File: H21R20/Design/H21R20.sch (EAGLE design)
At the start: 52 parts, among them IC1 ESP32-C3-MINI-1-N4, P1 HEXABIT_17.32_NO_P6_P7_P12, U1 STM32G0B1CEU6NUFQFPN48_STM32_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, X1 8MHZ

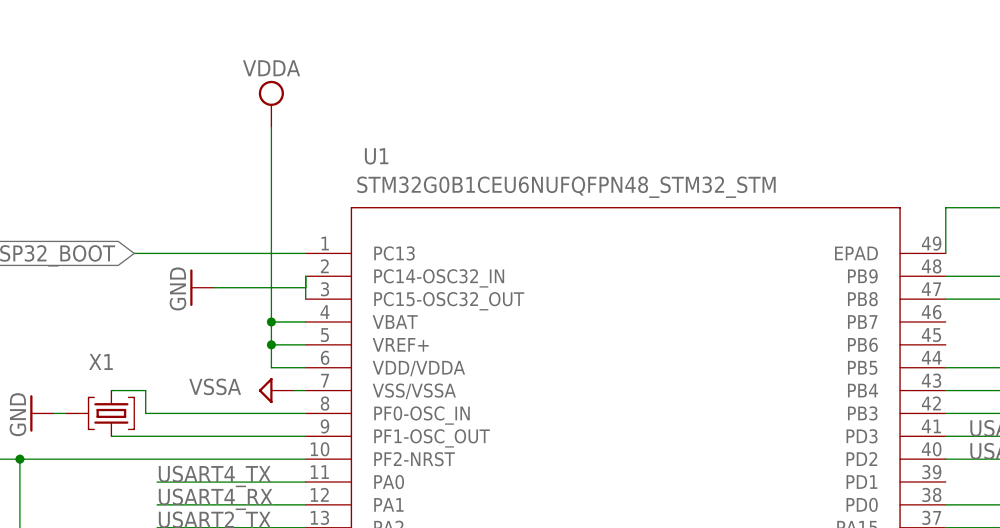
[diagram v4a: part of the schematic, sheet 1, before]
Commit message: -Improve the layout design -Change the jumber resistors footprint to 0402
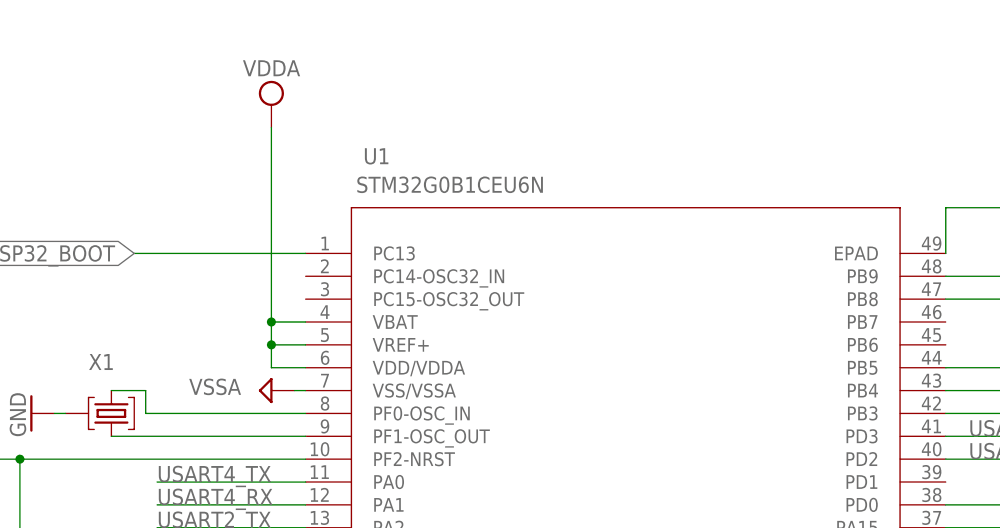
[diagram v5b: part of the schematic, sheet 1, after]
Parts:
- R11, R12, R13: device HEXABITZ_RCLS:R-0603 -> HEXABITZ_RCLS:R-0402
- U1: value STM32G0B1CEU6NUFQFPN48_STM32_STM -> STM32G0B1CEU6N; device HEXABITZ_ICs:STM32G0B1CEU6NUFQFPN48_STM32_STM -> HEXABITZ_ICs:STM32G0B1CEU6N; OCTOPART_URL https://octopart.com/stm32g0b1ceu6n-stmicroelectronics-1163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 -> (none)
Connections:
- net GND: no longer U1.PC14-OSC32_IN, U1.PC15-OSC32_OUT
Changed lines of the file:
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@@
 <?xml version="1.0" encoding="utf-8"?>
 <!DOCTYPE eagle SYSTEM "eagle.dtd">
-<eagle version="9.6.1">
+<eagle version="9.6.2">
 <drawing>
 <settings>
@@
 <layer number="1" name="Top" color="4" fill="1" visible="no" active="no"/>
 <layer number="2" name="Route2" color="1" fill="3" visible="no" active="no"/>
+<layer number="3" name="Route3" color="17" fill="1" visible="no" active="no"/>
+<layer number="4" name="Route4" color="18" fill="1" visible="no" active="no"/>
+<layer number="5" name="Route5" color="19" fill="1" visible="no" active="no"/>
+<layer number="6" name="Route6" color="25" fill="1" visible="no" active="no"/>
+<layer number="7" name="Route7" color="26" fill="1" visible="no" active="no"/>
+<layer number="8" name="Route8" color="27" fill="1" visible="no" active="no"/>
+<layer number="9" name="Route9" color="28" fill="1" visible="no" active="no"/>
+<layer number="10" name="Route10" color="29" fill="1" visible="no" active="no"/>
+<layer number="11" name="Route11" color="30" fill="1" visible="no" active="no"/>
+<layer number="12" name="Route12" color="20" fill="1" visible="no" active="no"/>
+<layer number="13" name="Route13" color="21" fill="1" visible="no" active="no"/>
+<layer number="14" name="Route14" color="22" fill="1" visible="no" active="no"/>
 <layer number="15" name="Route15" color="4" fill="6" visible="no" active="no"/>
 <layer number="16" name="Bottom" color="1" fill="1" visible="no" active="no"/>
@@
 <part name="SUPPLY12" library="supply2" library_urn="urn:adsk.eagle:library:372" deviceset="VCC" device="" value="VDDA"/>
 <part name="SUPPLY9" library="supply2" library_urn="urn:adsk.eagle:library:372" deviceset="GND1" device="" value="VSSA"/>
-<part name="U1" library="HEXABITZ_ICs" library_urn="urn:adsk.eagle:library:20064554" deviceset="STM32G0B1CEU6N" device="UFQFPN48_STM32_STM" package3d_urn="urn:adsk.eagle:package:33906703/4">
-<attribute name="OCTOPART_URL" value="https://octopart.com/stm32g0b1ceu6n-stmicroelectronics-116364672?r=sp"/>
-</part>
+<part name="U1" library="HEXABITZ_ICs" library_urn="urn:adsk.eagle:library:20064554" deviceset="STM32G0B1CEU6N" device="" package3d_urn="urn:adsk.eagle:package:39679334/7" value="STM32G0B1CEU6N"/>
 <part name="R" library="HEXABITZ_USER_INTERFACE_PARTS" library_urn="urn:adsk.eagle:library:20064563" deviceset="PINHD-1X1" device="" package3d_urn="urn:adsk.eagle:package:22485/2"/>
 <part name="JP1" library="pinhead" deviceset="PINHD-1X3" device="" package3d_urn="urn:adsk.eagle:package:22458/2"/>
@@
 <part name="RX0" library="HEXABITZ_CONNECTION_PARTS" library_urn="urn:adsk.eagle:library:27886345" deviceset="PAD4" device="" package3d_urn="urn:adsk.eagle:package:27886422/1"/>
 <part name="TX0" library="HEXABITZ_CONNECTION_PARTS" library_urn="urn:adsk.eagle:library:27886345" deviceset="PAD4" device="" package3d_urn="urn:adsk.eagle:package:27886422/1"/>
-<part name="R11" library="HEXABITZ_RCLS" library_urn="urn:adsk.eagle:library:20064561" deviceset="R-0603" device="" package3d_urn="urn:adsk.eagle:package:1435818/5" value="0R">
+<part name="R11" library="HEXABITZ_RCLS" library_urn="urn:adsk.eagle:library:20064561" deviceset="R-0402" device="" package3d_urn="urn:adsk.eagle:package:19666455/3" value="0R">
 <attribute name="MFN" value="YAGEO [VR]"/>
 <attribute name="MPN" value="RC0603JR-070RL"/>
@@
 <attribute name="RESISTANCE" value="0R"/>
 </part>
-<part name="R12" library="HEXABITZ_RCLS" library_urn="urn:adsk.eagle:library:20064561" deviceset="R-0603" device="" package3d_urn="urn:adsk.eagle:package:1435818/5" value="0R">
+<part name="R12" library="HEXABITZ_RCLS" library_urn="urn:adsk.eagle:library:20064561" deviceset="R-0402" device="" package3d_urn="urn:adsk.eagle:package:19666455/3" value="0R">
 <attribute name="MFN" value="YAGEO [VR]"/>
 <attribute name="MPN" value="RC0603JR-070RL"/>
@@
 <attribute name="RESISTANCE" value="0R"/>
 </part>
-<part name="R13" library="HEXABITZ_RCLS" library_urn="urn:adsk.eagle:library:20064561" deviceset="R-0603" device="" package3d_urn="urn:adsk.eagle:package:1435818/5" value="0R">
+<part name="R13" library="HEXABITZ_RCLS" library_urn="urn:adsk.eagle:library:20064561" deviceset="R-0402" device="" package3d_urn="urn:adsk.eagle:package:19666455/3" value="0R">
 <attribute name="MFN" value="YAGEO [VR]"/>
 <attribute name="MPN" value="RC0603JR-070RL"/>
@@
 <attribute name="VOLTAGE_RATING" value="16.0 V"/>
 </part>
-<part name="GND4" library="supply1" library_urn="urn:adsk.eagle:library:371" deviceset="GND" device=""/>
 </parts>
 <sheets>
@@
 <attribute name="VALUE" x="262.89" y="134.62" size="1.778" layer="96"/>
 </instance>
-<instance part="GND4" gate="1" x="130.81" y="171.45" smashed="yes" rot="R270">
-<attribute name="VALUE" x="128.42875" y="173.83125" size="1.778" layer="96" rot="R270"/>
-</instance>
 </instances>
 <busses>
@@
 <junction x="142.24" y="116.84"/>
 </segment>
-<segment>
-<pinref part="GND4" gate="1" pin="GND"/>
-<wire x1="133.35" y1="171.45" x2="143.51" y2="171.45" width="0.1524" layer="91"/>
-<pinref part="U1" gate="A" pin="PC14-OSC32_IN"/>
-<wire x1="143.51" y1="171.45" x2="143.51" y2="172.72" width="0.1524" layer="91"/>
-<pinref part="U1" gate="A" pin="PC15-OSC32_OUT"/>
-<wire x1="143.51" y1="172.72" x2="143.51" y2="170.18" width="0.1524" layer="91"/>
-</segment>
 </net>
